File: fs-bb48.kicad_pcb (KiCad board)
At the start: 2 copper layers, 12 parts, among them P2 SWD, P3 PWR, P4 EXT, U1 MKL27Z256VFM4

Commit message: add footprints
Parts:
- added P1: USB, fs-bb48:usb-PCB, F.Cu at (126.5, 106.9)
- added T1: TOUCH_PAD, fs-bb48:TOUCH_PAD_9mm, F.Cu at (154.9, 106.9)
- added U2: EMIF02-USB03F2, fs-bb48:BGA-11, F.Cu at (136.9, 105.3)
- moved FB1 13.9 mm to (136.9, 110.0), turned to 0 degrees
- moved C1 12.2 mm to (136.9, 107.6), turned to 90 degrees
- moved P2 10.4 mm to (145.5, 112.0), turned to 270 degrees
- moved C3 10.3 mm to (138.7, 108.0), turned to 270 degrees
- moved C2 9.01 mm to (138.7, 105.2), turned to 90 degrees
- moved C4 8.21 mm to (144.3, 110.1), turned to 0 degrees
- moved P3 7.91 mm to (148.1, 104.4), turned to 180 degrees
- moved R1 7.82 mm to (148.3, 110.0), turned to 0 degrees
- moved D1 5.85 mm to (147.6, 108.5)
- moved R2 5.24 mm to (148.3, 106.9), turned to 180 degrees
- moved P4 4.02 mm to (145.5, 101.9), turned to 270 degrees
- moved U1 3.82 mm to (143.0, 106.4), turned to 0 degrees
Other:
- board outline added: 35 x 12.1 mm

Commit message: update
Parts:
- moved C2 3.66 mm to (138.7, 108.8), turned to 270 degrees
- moved C1 3.59 mm to (138.6, 104.4), turned to 0 degrees
- moved C3 1.80 mm to (136.9, 108.0)
- moved U2 0.77 mm to (136.4, 105.9)
- moved D1 0.23 mm to (147.8, 108.5)
- moved U1 0.05 mm to (143.1, 106.4)
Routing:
- net GND: track 0.00 -> 60.1 mm, vias 0 -> 2
- net +3V3: track 0.00 -> 27.6 mm, vias 0 -> 3
- net Net-(R2-Pad2): track 0.00 -> 10.5 mm, vias 0 -> 2
- net Net-(C1-Pad1): track 0.00 -> 10.5 mm, vias 0 -> 3
- net Net-(P1-Pad2): track 0.00 -> 6.27 mm
- net Net-(P2-Pad1): track 0.00 -> 5.71 mm
- net Net-(FB1-Pad1): track 0.00 -> 5.13 mm
- net Net-(P1-Pad3): track 0.00 -> 5.05 mm
- net Net-(P4-Pad4): track 0.00 -> 4.52 mm
- net Net-(P4-Pad1): track 0.00 -> 4.00 mm
- net Net-(P2-Pad2): track 0.00 -> 3.86 mm
- net Net-(U1-Pad4): track 0.00 -> 3.76 mm
- net Net-(U1-Pad3): track 0.00 -> 3.76 mm
- net Net-(P2-Pad3): track 0.00 -> 3.72 mm
- net Net-(P4-Pad3): track 0.00 -> 2.86 mm
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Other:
- net class VBUS added: clearance 0.2, trace_width 0.35, via_dia 0.6, via_drill 0.4

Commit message: update
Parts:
- U1: footprint Housings_DFN_QFN:QFN-32-1EP_5x5mm_Pitch0.5mm -> fs-bb48:QFN-32-1EP_5x5mm_Pitch0.5mm
- moved U2 0.46 mm to (136.4, 105.4)

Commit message: more update
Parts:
- C1, C2: footprint Capacitors_SMD:C_0603 -> fs-bb48:C_0603
- C3: footprint Capacitors_SMD:C_0402 -> fs-bb48:C_0402
- D1: footprint LEDs:LED-0603 -> fs-bb48:LED-0603
- FB1: footprint Inductors_NEOSID:Neosid_Inductor_SM0603CG -> fs-bb48:Inductor_SM0603
- P2: footprint Pin_Headers:Pin_Header_Straight_1x04 -> fs-bb48:Pin_Header_Straight_1x04_A
- P3: footprint Pin_Headers:Pin_Header_Straight_1x02 -> fs-bb48:Pin_Header_Straight_1x02
- P4: footprint Pin_Headers:Pin_Header_Straight_1x04 -> fs-bb48:Pin_Header_Straight_1x04
- R1, R2: footprint Resistors_SMD:R_0402 -> fs-bb48:R_0402
- moved C4 0.89 mm to (145.2, 110.1)
- moved D1 0.86 mm to (148.2, 109.2)
- moved R1 0.68 mm to (148.1, 110.6), turned to 180 degrees
- moved R2 0.52 mm to (148.5, 107.4)
- moved U1 0.46 mm to (143.5, 106.4)
- moved C3 0.28 mm to (137.2, 108.0)
- moved C1 0.23 mm to (138.8, 104.4)
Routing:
- net +3V3: track 27.6 -> 36.8 mm
- net GND: track 60.1 -> 62.0 mm
- net Net-(D1-Pad1): track 2.79 -> 3.78 mm
- net Net-(P4-Pad4): track 4.52 -> 5.50 mm
- net Net-(P1-Pad2): track 6.27 -> 5.49 mm
- net Net-(P2-Pad3): track 3.72 -> 4.47 mm
- net Net-(C1-Pad1): track 10.5 -> 11.0 mm
- added copper zone on B.Cu, net GND
- added copper zone on F.Cu, net GND

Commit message: update
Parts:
- added FST-LOGO: VAL**, fs-bb48:FST-LOGO, B.Cu at (159.0, 106.7)
- added H1: 2mm, fs-bb48:Hole, F.Cu at (159.8, 102.6)
- FB1: value 330Ohm -> 330ohm
- moved R2 0.80 mm to (148.2, 106.7)
- moved D1 0.74 mm to (147.6, 108.8), turned to 270 degrees
- moved R1 0.32 mm to (148.1, 110.9), turned to 0 degrees
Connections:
- net Net-(C1-Pad1) renamed /VBUS
- net Net-(D1-Pad1) renamed /LED
- net Net-(FB1-Pad1) renamed /VBUS_
- net Net-(P1-Pad2) renamed /D-_
- net Net-(P1-Pad3) renamed /D+_
- net Net-(P2-Pad1) renamed /RESET
- net Net-(P2-Pad2) renamed /SWD_DIO
- net Net-(P2-Pad3) renamed /SWD_CLK
- net Net-(P4-Pad1) renamed /PTD4
- net Net-(P4-Pad2) renamed /PTD5
- net Net-(P4-Pad3) renamed /PTD6
- net Net-(P4-Pad4) renamed /PTD7
- net Net-(R2-Pad2) renamed /TOUCH
- net Net-(U1-Pad3) renamed /D+
- net Net-(U1-Pad4) renamed /D-
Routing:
- net GND: track 62.0 -> 56.4 mm
- net +3V3: track 36.8 -> 32.8 mm
- net /LED: track 3.78 -> 2.52 mm
- net /D+_: track 5.05 -> 4.08 mm
- net /TOUCH: track 10.8 -> 9.92 mm
- net /PTD7: track 5.50 -> 6.27 mm
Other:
- net class GND added: clearance 0.2, trace_width 0.7, via_dia 0.6, via_drill 0.4
- board text added: "FS-BB48"
- board text added: "Flying Stone Technology"

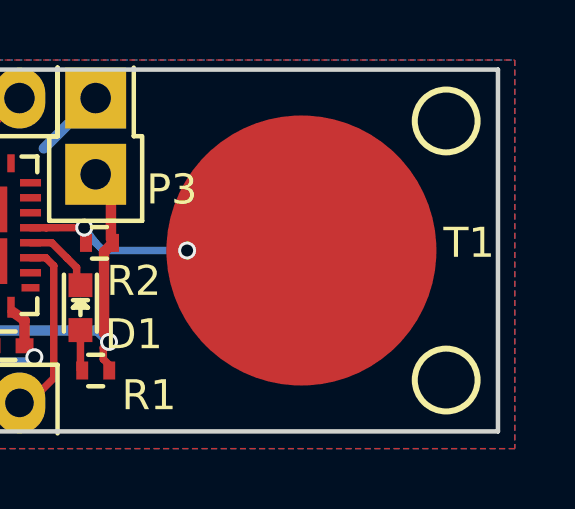
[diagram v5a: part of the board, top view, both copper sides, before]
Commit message: fix hole size
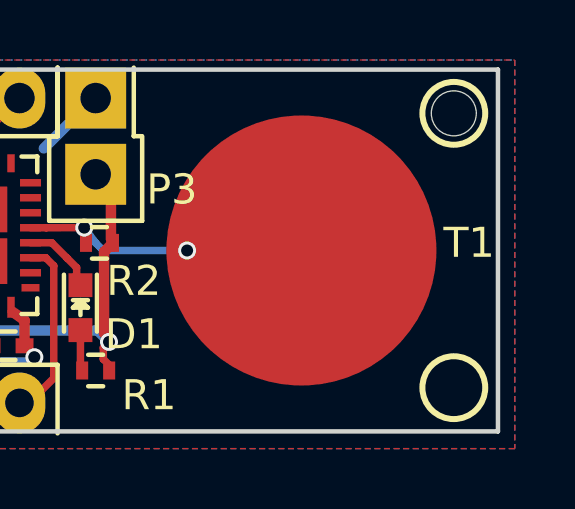
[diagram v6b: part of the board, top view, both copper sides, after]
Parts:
- moved H1 0.36 mm to (160.0, 102.4)
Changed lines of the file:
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@@
     (links 37)
     (no_connects 0)
-    (area 122.827 95.395 165.914524 116.799)
+    (area 122.827 95.395 164.390619 116.799)
     (thickness 2)
     (drawings 8)
@@
   (layers
     (0 F.Cu signal)
-    (31 B.Cu signal hide)
+    (31 B.Cu signal)
     (32 B.Adhes user)
     (33 F.Adhes user)
@@
     (35 F.Paste user)
     (36 B.SilkS user hide)
-    (37 F.SilkS user hide)
+    (37 F.SilkS user)
     (38 B.Mask user)
     (39 F.Mask user)
@@
     (pad_to_mask_clearance 0.2)
     (aux_axis_origin 154.94 106.68)
+    (grid_origin 154.94 106.68)
     (visible_elements 7FFFFB97)
     (pcbplotparams
@@
       (drillshape 0)
       (scaleselection 1)
-      (outputdirectory ""))
+      (outputdirectory tmp/))
   )
   (net 0 "")
@@
     )
   )
-  (module fs-bb48:Hole (layer F.Cu)
-    (at 159.766 102.616)
-    (fp_text reference H1 (at 3.302 0.254) (layer F.SilkS) hide
-      (effects (font (size 1 1) (thickness 0.15)))
-    )
-    (fp_text value 2mm (at 4.064 -1.27) (layer F.Fab) hide
-      (effects (font (size 1 1) (thickness 0.15)))
-    )
-    (pad "" np_thru_hole circle (at 0 0) (size 2 2) (drill 2) (layers *.Cu *.Mask F.SilkS))
-  )
   (module fs-bb48:BGA-11 (layer F.Cu)
     (at 136.398 105.41)
@@
       (solder_mask_margin 0.025) (solder_paste_margin 0.025) (clearance 0.05))
   )
+  (module fs-bb48:Hole (layer F.Cu)
+    (at 160.02 102.362)
+    (fp_text reference H1 (at 2.54 1.524) (layer F.SilkS) hide
+      (effects (font (size 1 1) (thickness 0.15)))
+    )
+    (fp_text value 2mm (at 2.032 -1.27) (layer F.Fab) hide
+      (effects (font (size 1 1) (thickness 0.15)))
+    )
+    (pad "" np_thru_hole circle (at 0 0) (size 1.5 1.5) (drill 1.5) (layers *.Cu *.Mask F.SilkS))
+  )
   (gr_text FS-BB48 (at 154.178 102.87) (layer B.SilkS)
     (effects (font (size 1.2 1.2) (thickness 0.3) italic) (justify mirror))
@@
     (effects (font (size 1.5 1.5) (thickness 0.3)) (justify mirror))
   )
-  (gr_circle (center 159.766 102.616) (end 158.75 102.362) (layer F.SilkS) (width 0.2))
-  (gr_circle (center 159.766 111.252) (end 158.75 110.998) (layer F.SilkS) (width 0.2))
+  (gr_circle (center 160.02 102.362) (end 159.004 102.108) (layer F.SilkS) (width 0.2))
+  (gr_circle (center 160.02 111.506) (end 159.004 111.252) (layer F.SilkS) (width 0.2))
   (gr_line (start 161.492 112.964) (end 126.492 112.964) (angle 90) (layer Edge.Cuts) (width 0.15))
   (gr_line (start 161.492 100.904) (end 161.492 112.964) (angle 90) (layer Edge.Cuts) (width 0.15))
